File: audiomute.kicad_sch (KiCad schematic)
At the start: 21 parts, among them J1 MJ-3523-SMT, J2 B2B-XH-A_LF__SN_, J3 B2B-XH-A_LF__SN_, J4 MJ-3523-SMT, Q1 NPN, Q2 PNP, Q3 NPN, Q4 NPN

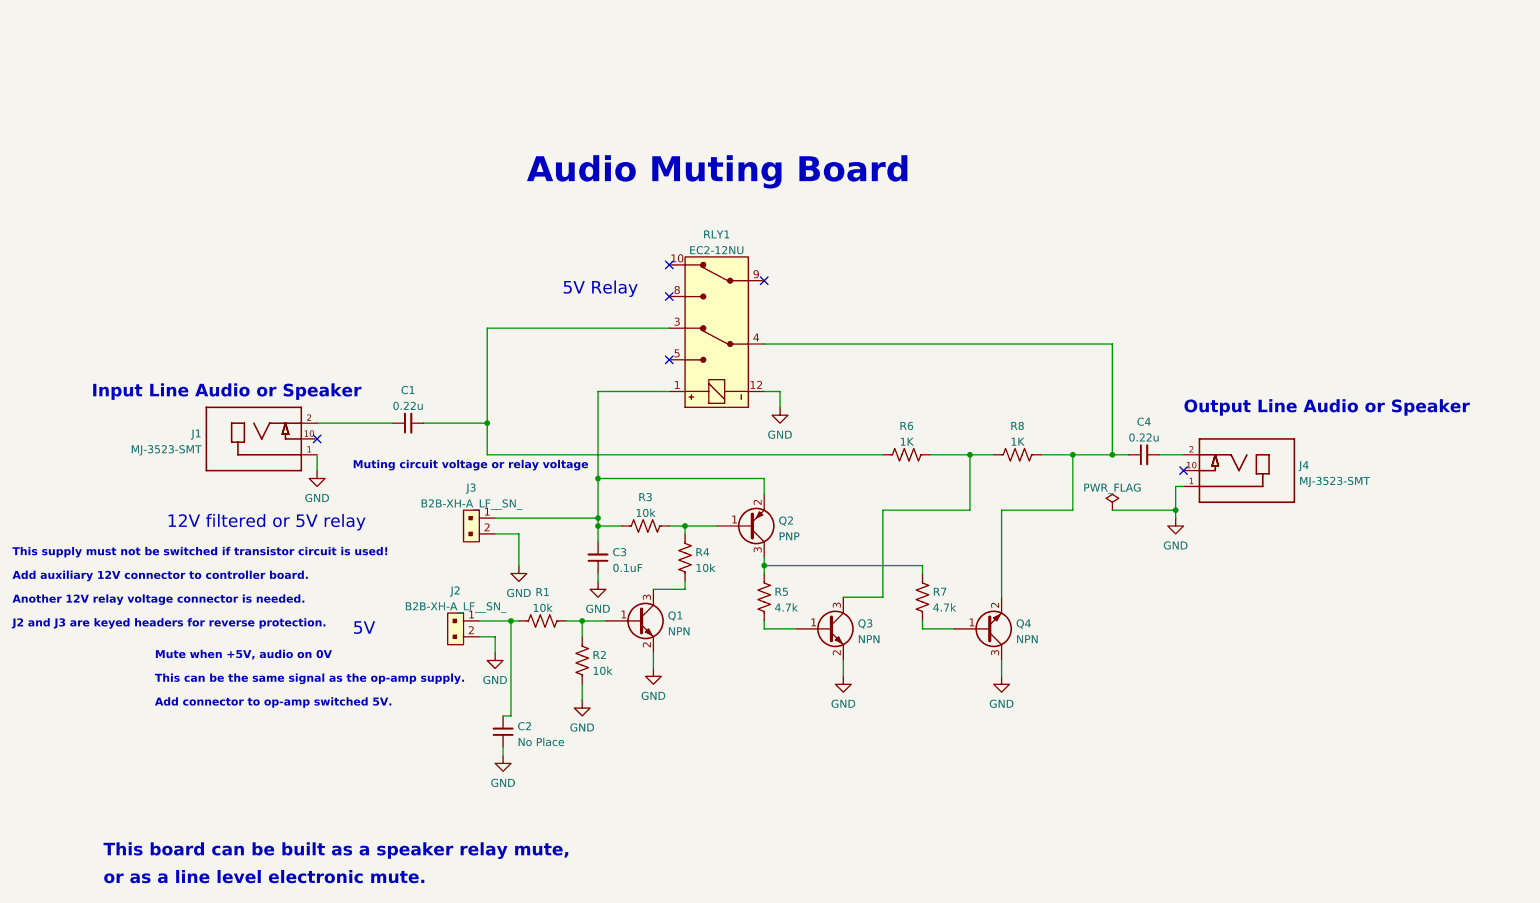
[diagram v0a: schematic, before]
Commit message: Finished version 1.0.  Ready to release PCB.
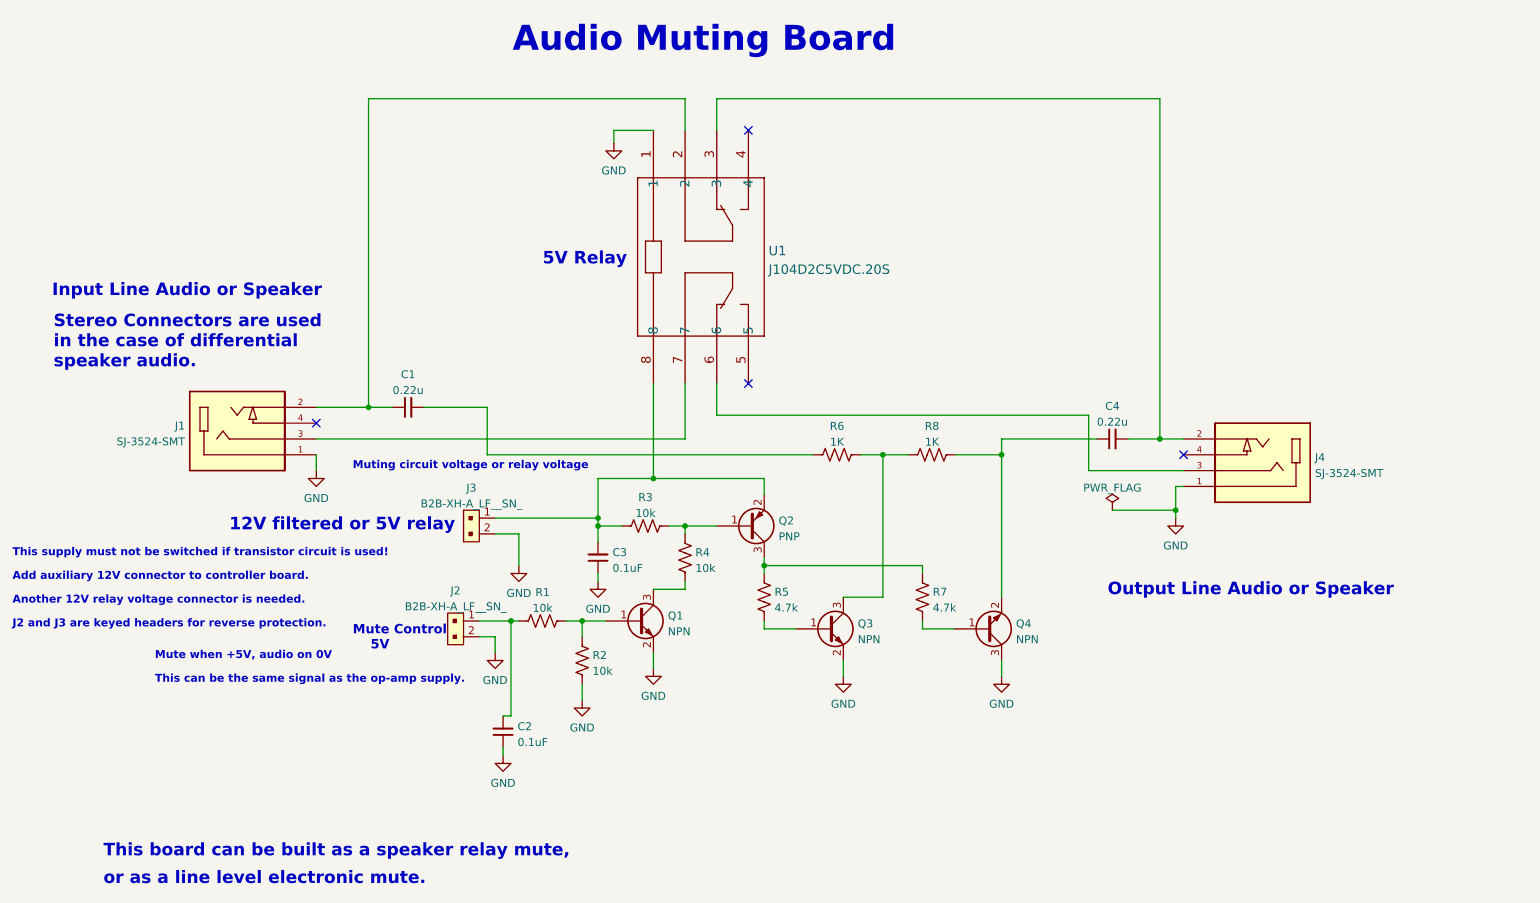
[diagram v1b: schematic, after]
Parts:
- removed J1, J4: MJ-3523-SMT, MJ-3523-SMT:CUI_MJ-3523-SMT, symbol MJ-3523-SMT:MJ-3523-SMT
- removed RLY1: EC2-12NU, digikey-footprints:Relay_THT_EC2, symbol dk_Signal-Relays-Up-to-2-Amps:EC2-12NU
- added J1, J4: SJ-3524-SMT, Stereo_Jack_SMT:CUI_SJ-3524-SMT, symbol Stereo_Jack_SMT:SJ-3524-SMT
- added U1: J104D2C5VDC.20S, Relay_DPDT_GP:J104D2C5VDC.20S, symbol Relay_DPDT_general:J104D2C5VDC.20S
- C2: value No Place -> 0.1uF
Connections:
- net GND: now also J1.1, J4.1, U1.1
- net at C3.2, J3.1, Q2.2 (E)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: now also U1.8
- net at C1.1: now also J1.2, U1.2
- net at C4.2: now also J4.2, U1.3
- new net: J4.3, U1.6
- new net: J1.3, U1.7
- no-connect marks 6 -> 4
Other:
- note added: "Mute Control 5V"
- note added: "Stereo Connectors are used in the case of differential speaker audio."
- note removed: "5V"
- note removed: "Add connector to op-amp switched 5V."
- moved on the sheet: C1, C4, R6, R8

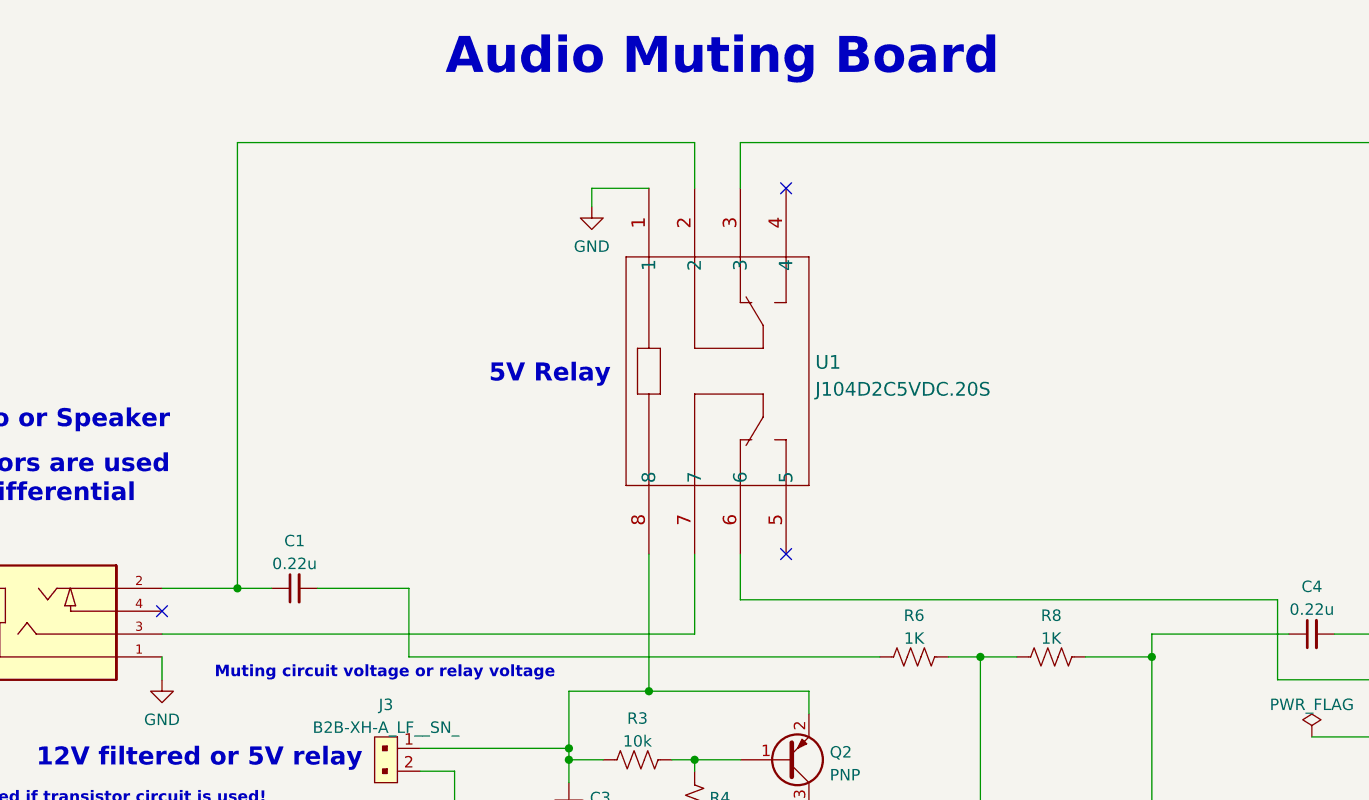
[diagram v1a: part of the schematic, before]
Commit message: Revised board uses larger relay, and has differential input and output.
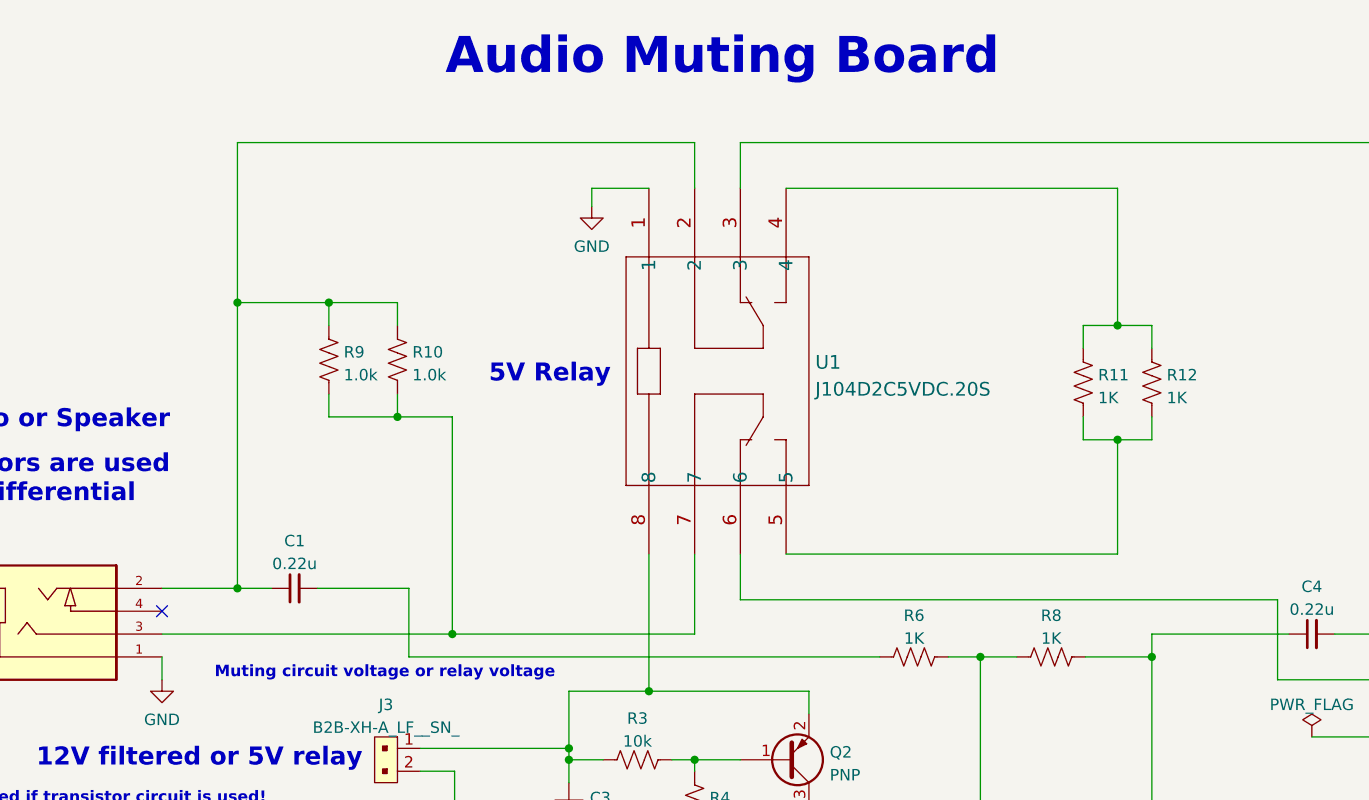
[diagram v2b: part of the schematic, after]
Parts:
- added R10, R9: 1.0k, Resistor_SMD:R_1206_3216Metric_Pad1.30x1.75mm_HandSolder, symbol Device:R_US
- added R11, R12: 1K, Resistor_SMD:R_1206_3216Metric_Pad1.30x1.75mm_HandSolder, symbol Device:R_US
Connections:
- net at C1.1, J1.2, U1.2: now also R10.1, R9.1
- net at U1.4: now also R11.2, R12.2
- net at U1.5: now also R11.1, R12.1
- net at J1.3, U1.7: now also R10.2, R9.2
- no-connect marks 4 -> 2
